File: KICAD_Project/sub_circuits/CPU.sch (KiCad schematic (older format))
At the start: 5 parts, among them P201 MPC5554, SW201 SWITCH_INV, SW202 PUSH_B3S

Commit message: changed stepper from L297 to A4988 from pololu
Signed-off-by: Jared Harvey <TortiseGIT@jaredharvey.com>
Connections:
- net labels added: A4988_CCW, A4988_CLK, A4988_EN
- net labels removed: L297_CCW, L297_CLK, L297_EN
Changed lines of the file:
@@
-EESchema Schematic File Version 2  date 9/27/2011 11:45:22 AM
+EESchema Schematic File Version 2  date 10/2/2011 8:46:35 AM
 LIBS:power
 LIBS:device
@@
 $Descr D 34000 22000
 encoding utf-8
-Sheet 2 13
+Sheet 2 12
 Title "freeEMS PLUS from Cinch template "
-Date "27 sep 2011"
+Date "2 oct 2011"
 Rev "A-DRAFT5"
 Comp "diyefi.org/openecu.info"
@@
 MC10XS3412_IN0_DIGI
 Text HLabel 23850 2300 0    60   Input ~ 0
-L297_CLK
+A4988_CLK
 Text HLabel 25350 2100 2    60   Input ~ 0
-L297_CCW
+A4988_CCW
 Text HLabel 23850 2200 0    60   Input ~ 0
 MC33800_P5_DIGI
@@
 MC33926_EN_DIGI
 Text HLabel 23850 17600 0    60   Input ~ 0
-L297_EN
+A4988_EN
 Text HLabel 25300 20000 2    60   Input ~ 0
 12_IGN_DIGI

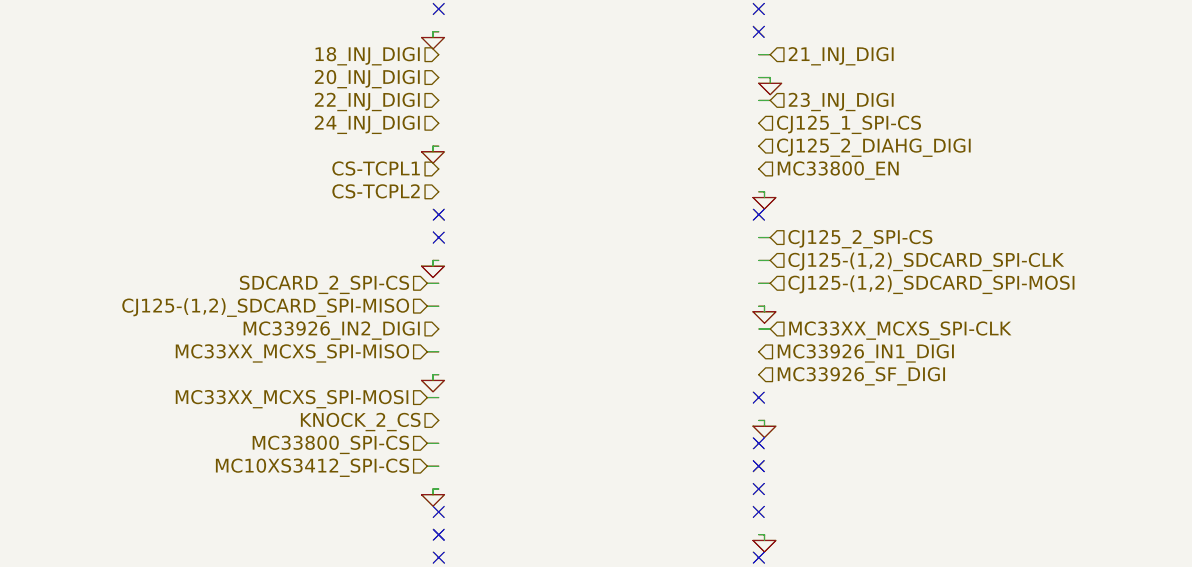
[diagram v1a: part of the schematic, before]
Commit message: Added some simulations for the AN protect lines
Signed-off-by: Jared Harvey <TortiseGIT@jaredharvey.com>
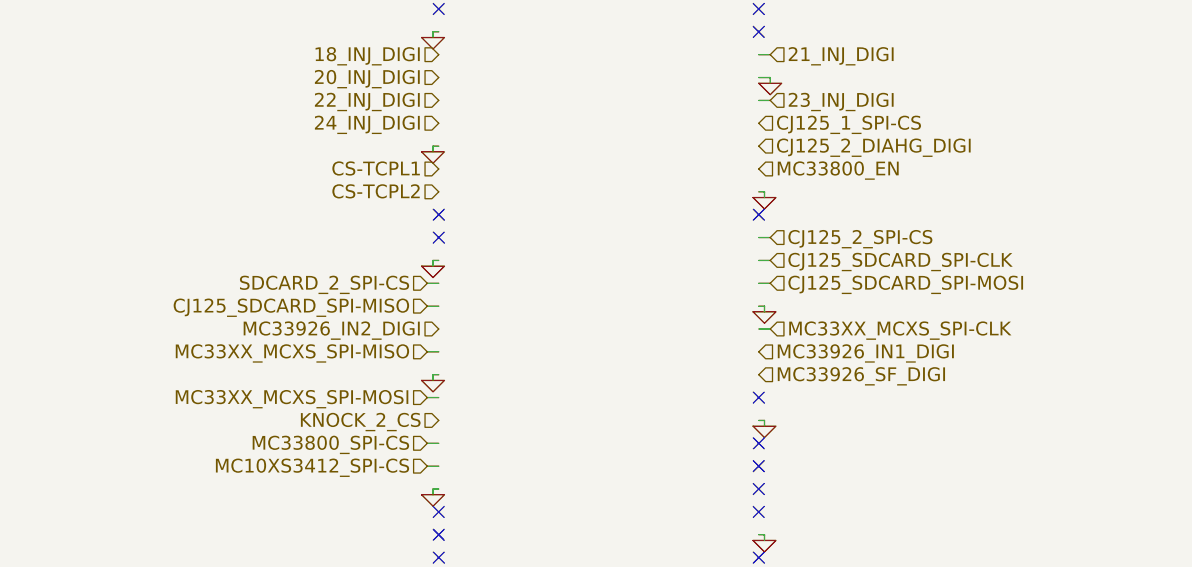
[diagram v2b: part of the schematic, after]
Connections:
- net labels added: CJ125_SDCARD_SPI-CLK, CJ125_SDCARD_SPI-MISO, CJ125_SDCARD_SPI-MOSI
- net labels removed: CJ125-(1,2)_SDCARD_SPI-CLK, CJ125-(1,2)_SDCARD_SPI-MISO, CJ125-(1,2)_SDCARD_SPI-MOSI
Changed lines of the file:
@@
-EESchema Schematic File Version 2  date 10/2/2011 8:46:35 AM
+EESchema Schematic File Version 2  date 10/4/2011 8:27:03 PM
 LIBS:power
 LIBS:device
@@
 Sheet 2 12
 Title "freeEMS PLUS from Cinch template "
-Date "2 oct 2011"
+Date "5 oct 2011"
 Rev "A-DRAFT5"
 Comp "diyefi.org/openecu.info"
@@
 MC33XX_MCXS_SPI-CLK
 Text HLabel 25350 5600 2    60   Input ~ 0
-CJ125-(1,2)_SDCARD_SPI-MOSI
+CJ125_SDCARD_SPI-MOSI
 Text HLabel 23850 5700 0    60   Input ~ 0
-CJ125-(1,2)_SDCARD_SPI-MISO
+CJ125_SDCARD_SPI-MISO
 Text HLabel 25350 5500 2    60   Input ~ 0
-CJ125-(1,2)_SDCARD_SPI-CLK
+CJ125_SDCARD_SPI-CLK
 Text HLabel 23850 5600 0    60   Input ~ 0
 SDCARD_2_SPI-CS
